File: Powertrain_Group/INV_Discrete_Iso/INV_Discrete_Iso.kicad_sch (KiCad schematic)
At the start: 21 parts, among them J1 Conn_01x04_Socket, J10 15130122601000, J2 Conn_01x04_Socket, J3 Conn_01x04_Socket, J4 Conn_01x04_Socket, J5 Conn_01x04_Socket, J6 Conn_01x04_Socket, J7 Conn_01x04_Socket, J8 Conn_01x04_Socket, J9 Conn_01x04_Socket

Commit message: [INV_Discrete_Iso] V1.1
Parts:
- J1: value Conn_01x04_Socket -> U_ISOPWR_H
- J10: value 15130122601000 -> Harting 15130122601000; footprint nturt_kicad_lib_EP6:15130122601000 -> nturt_kicad_lib_EP7:Harting_15130122601000; symbol nturt_kicad_lib_EP6:15130122601000 -> nturt_kicad_lib_EP7:Harting_15130122601000
- J2: value Conn_01x04_Socket -> U_PWM
- J3: value Conn_01x04_Socket -> U_ISOPWR_L
- J4: value Conn_01x04_Socket -> V_ISOPWR_H
- J5: value Conn_01x04_Socket -> V_PWM
- J6, J9: value Conn_01x04_Socket -> W_ISOPWR_L
- J7: value Conn_01x04_Socket -> W_ISOPWR_H
- J8: value Conn_01x04_Socket -> W_PWM
- R1: value 1K -> 10k
- R7: value 10k -> 22k
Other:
- note added: "V1.0 init by LY Chen V1.1 modify by Jack Kuo"
- company: (none) -> NTURacing
- title: (none) -> INV_Discrete_Iso
- moved on the sheet: J10

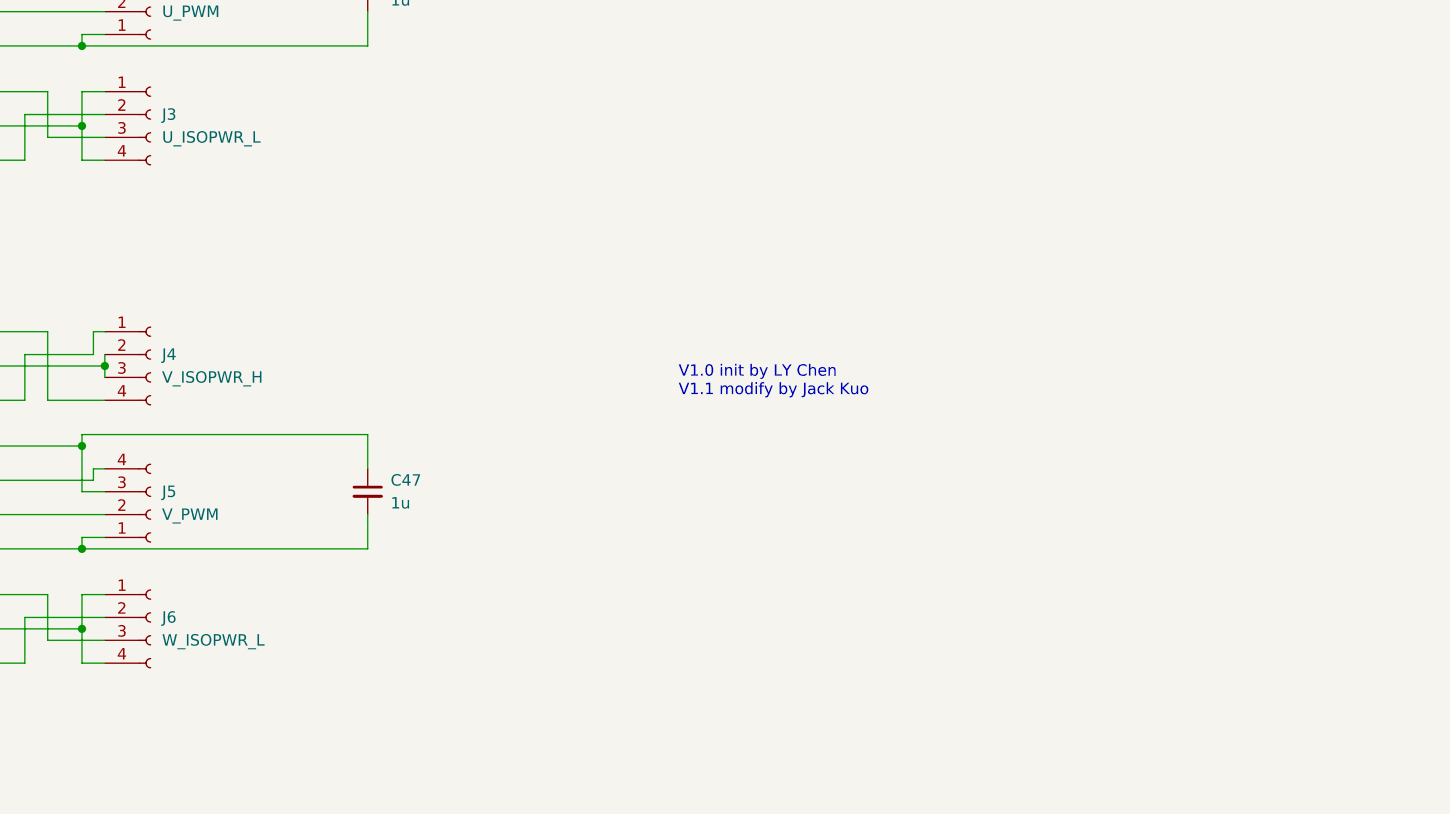
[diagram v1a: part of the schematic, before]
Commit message: [INV_Discrete_Iso] V1.2
fix connector to controller board mismatch
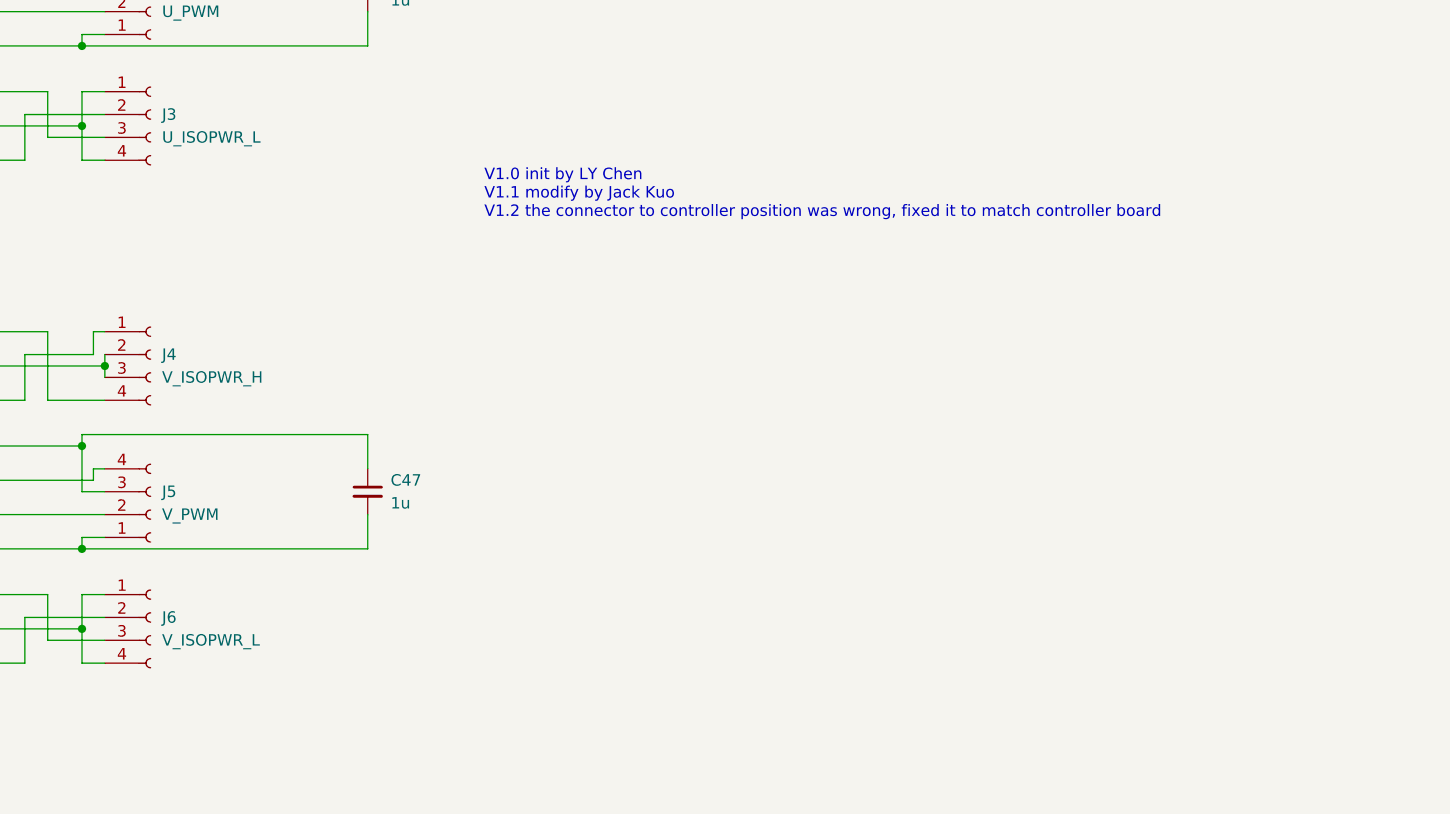
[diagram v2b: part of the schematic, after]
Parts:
- J6: value W_ISOPWR_L -> V_ISOPWR_L
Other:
- note added: "V1.0 init by LY Chen V1.1 modify by Jack Kuo V1.2 the connector to controller position was wrong, fixed it to match controller board"
- note removed: "V1.0 init by LY Chen V1.1 modify by Jack Kuo"
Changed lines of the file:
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@@
 	(title_block
 		(title "INV_Discrete_Iso")
-		(date "2026-03-14")
-		(rev "1.1")
+		(date "2026-03-18")
+		(rev "1.2")
 		(company "NTURacing")
 		(comment 1 "LY Chen")
@@
 		)
 	)
-	(text "V1.0 init by LY Chen\nV1.1 modify by Jack Kuo"
+	(text "V1.0 init by LY Chen\nV1.1 modify by Jack Kuo\nV1.2 the connector to controller position was wrong, fixed it to match controller board"
 		(exclude_from_sim no)
-		(at 212.344 86.36 0)
+		(at 190.754 64.516 0)
 		(effects
 			(font
@@
 			)
 		)
-		(property "Value" "W_ISOPWR_L"
+		(property "Value" "V_ISOPWR_L"
 			(at 154.94 116.8399 0)
 			(effects
